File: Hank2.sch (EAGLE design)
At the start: 44 parts

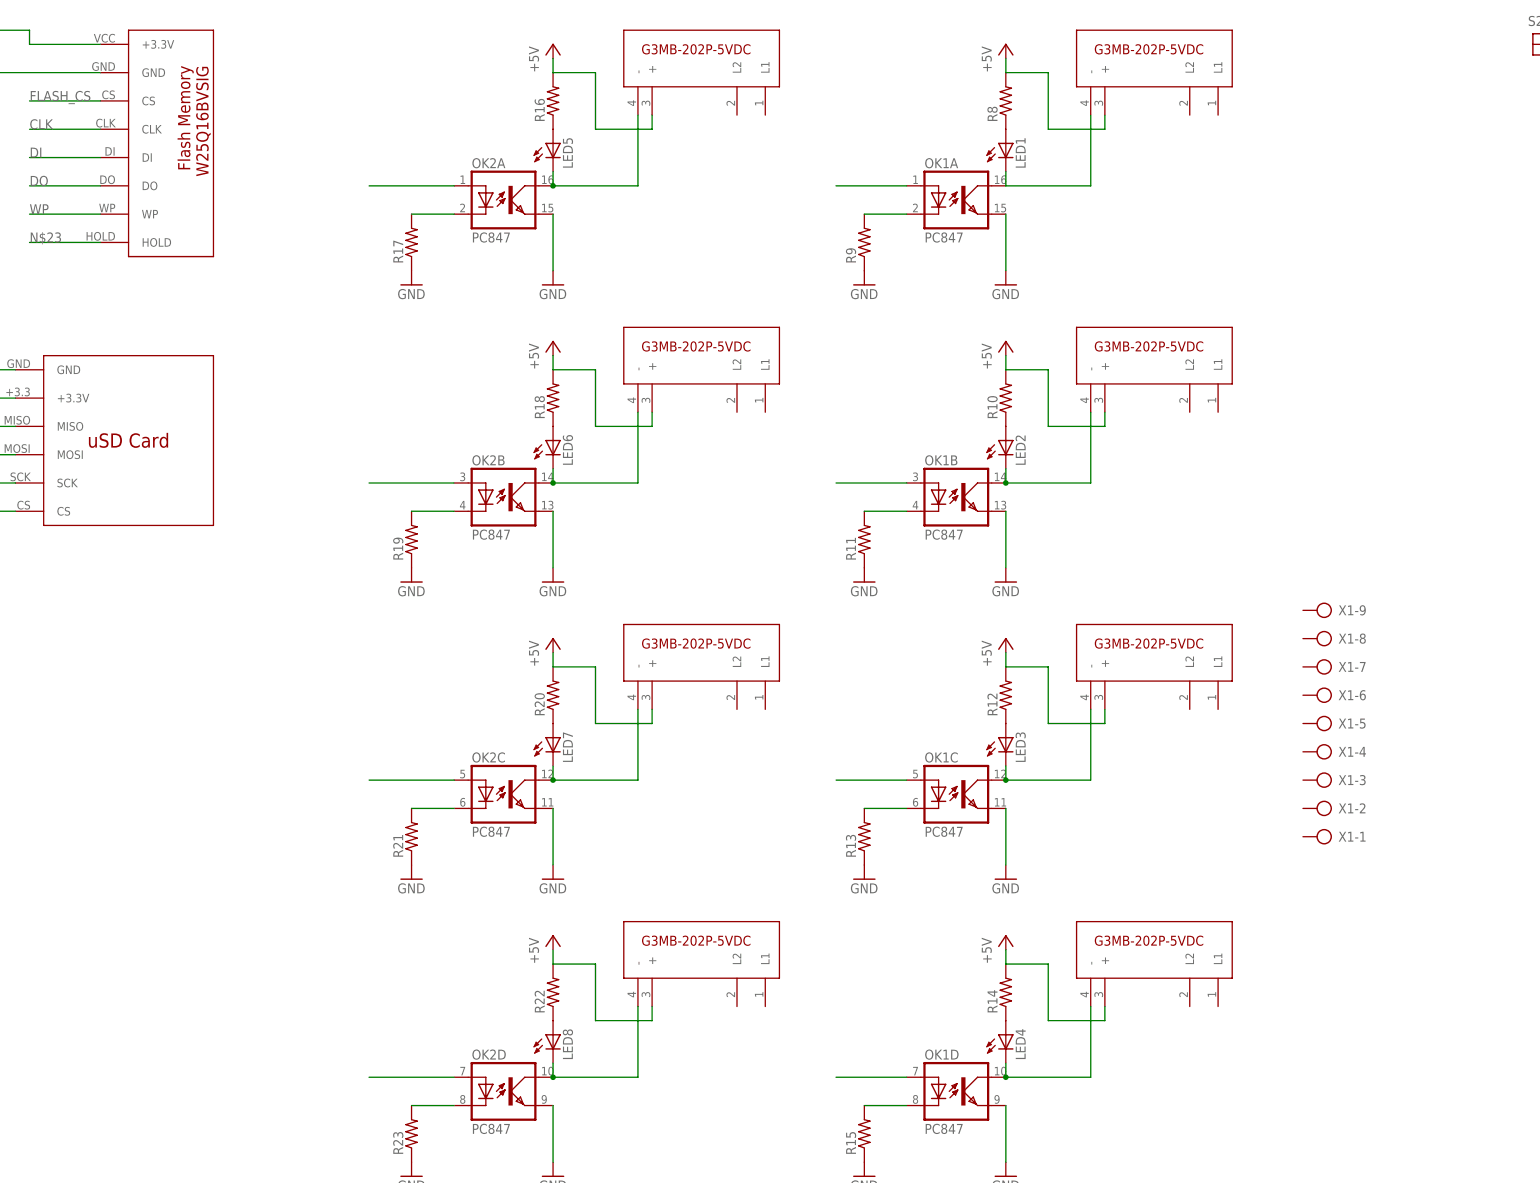
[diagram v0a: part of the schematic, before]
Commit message: Wired SSR circuits
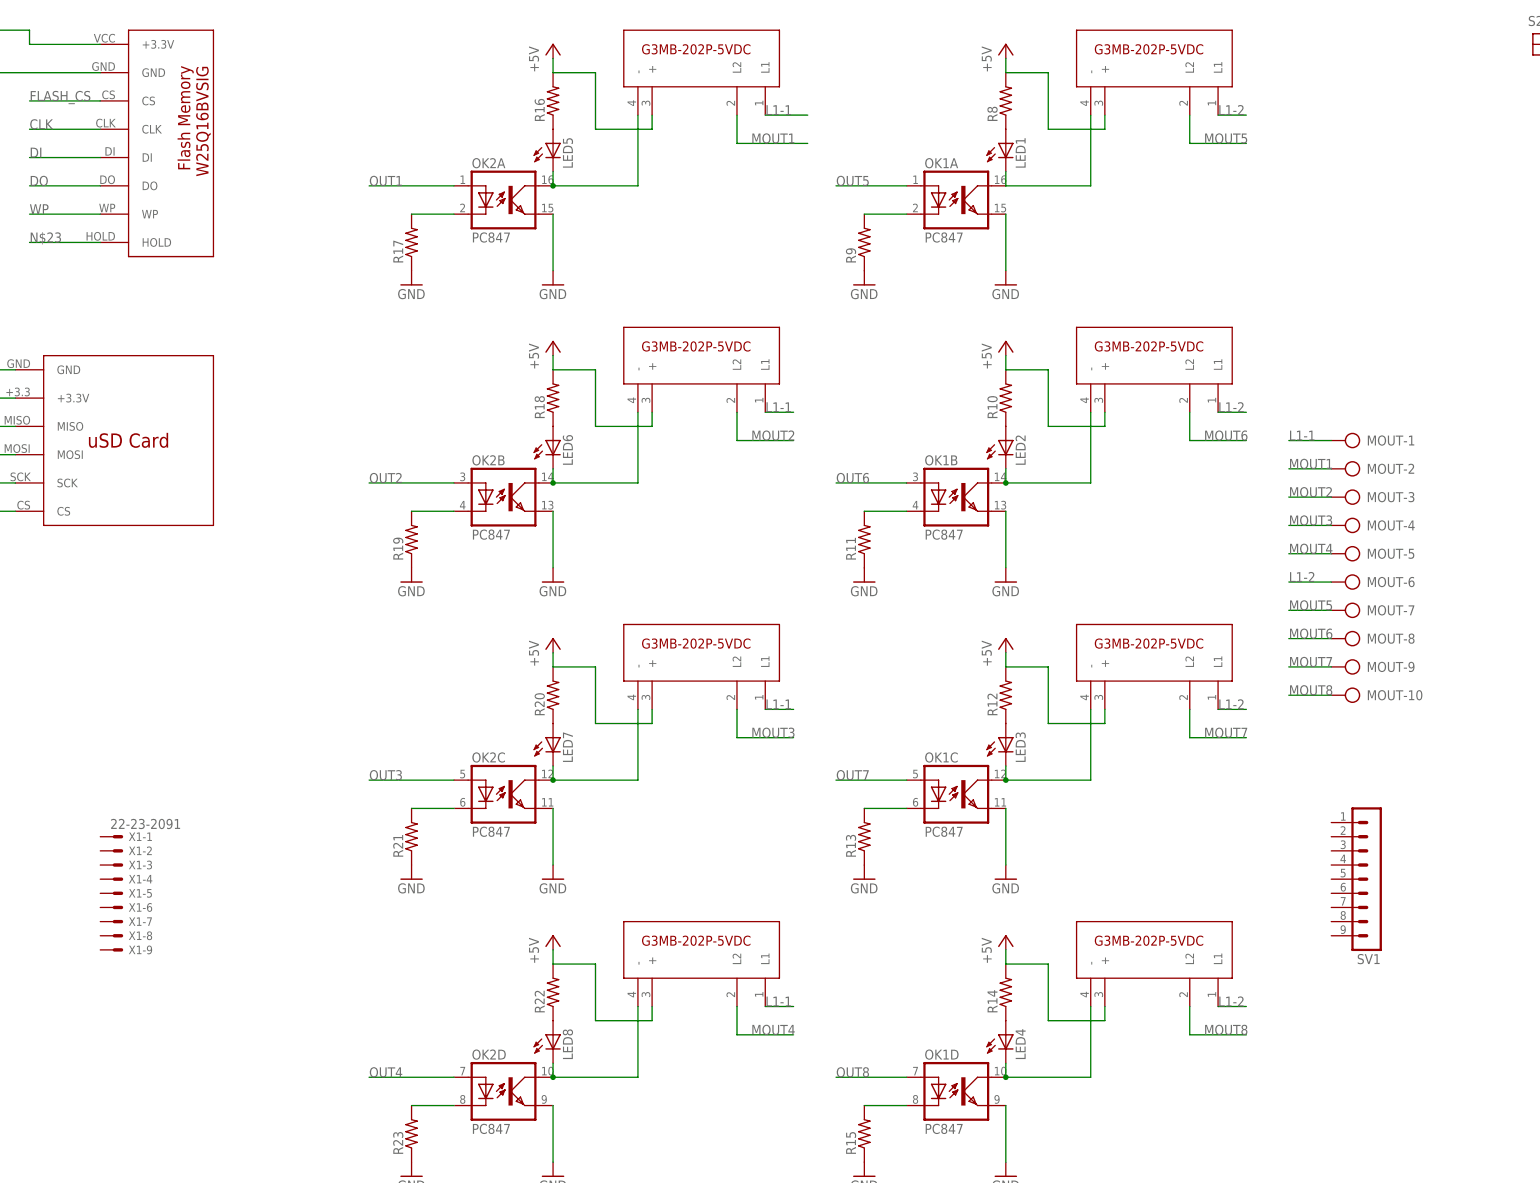
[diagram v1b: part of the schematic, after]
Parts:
- added MOUT: (no value), con-ptr500:AK300/10
- added SV1: (no value), con-lstb:MA09-1
- X1: value (none) -> 22-23-2091; device con-ptr500:AK300/9 -> con-molex:22-23-2091
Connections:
- net N$14 renamed OUT5
- net N$18 renamed OUT6
- net N$22 renamed OUT7
- net N$27 renamed OUT8
- net N$31 renamed OUT1
- net N$35 renamed OUT2
- net N$39 renamed OUT3
- net N$43 renamed OUT4
- new net L1-1: MOUT-1.KL, U$19.L1, U$20.L1, U$21.L1, U$22.L1
- new net L1-2: MOUT-6.KL, U$16.L1, U$17.L1, U$18.L1, U$8.L1
- new net MOUT1: MOUT-2.KL, U$19.L2
- new net MOUT2: MOUT-3.KL, U$20.L2
- new net MOUT3: MOUT-4.KL, U$21.L2
- new net MOUT4: MOUT-5.KL, U$22.L2
- new net MOUT5: MOUT-7.KL, U$8.L2
- new net MOUT6: MOUT-8.KL, U$16.L2
- new net MOUT7: MOUT-9.KL, U$17.L2
- new net MOUT8: MOUT-10.KL, U$18.L2
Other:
- moved on the sheet: X1-1, X1-2, X1-3, X1-4, X1-5, X1-6, X1-7, X1-8, X1-9

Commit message: Added microcontroller connections
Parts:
- added C1: 1000u, rcl:CPOL-USE5-8.5
- added C2: 0.1uF, rcl:C-US025-024X044
- added MIN, SV5: (no value), con-lstb:MA09-1
- added OLED_DISPLAY: (no value), con-lstb:MA04-1
- added PSU: (no value), con-ptr500:AK300/2
- added R1: 4.7K, rcl:R-US_0204/7
- added R2, R26: (no value), rcl:R-US_0204/7
- added R24, R25, R3, R4, R5, R6, R7: 330, rcl:R-US_0204/7
- added SV2: (no value), con-lstb:MA10-1
- added TEMP_SENSOR: (no value), con-lstb:MA03-1
- added X2: 22-23-2021, con-molex:22-23-2021
- added X3: Auto_Manual, con-molex:22-23-2021
- C5, C6, C7, C8: value (none) -> 0.1uF
- R10, R12, R14, R16, R18, R22, R8: value (none) -> 1k
- R11, R13, R15, R17, R19, R21, R23, R9: value (none) -> 150
- SV1: device con-lstb:MA09-1 -> con-lstb:MA10-1
- X1: value 22-23-2091 -> 22-23-2021; device con-molex:22-23-2091 -> con-molex:22-23-2021
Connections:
- removed net CLK: U$1.CLK
- removed net DI: U$1.DI
- removed net DO: U$1.DO
- removed net N$23: U$1.HOLD
- removed net WP: U$1.WP
- new net AUTO: R2.2, SV2.10, X3-2.S
- new net FLASH_CLK: SV2.2, U$1.CLK
- new net FLASH_DI: SV2.3, U$1.DI
- new net FLASH_DO: SV2.4, U$1.DO
- new net IN1: R3.1, SV5.2
- new net IN2: R4.1, SV5.3
- new net IN3: R5.1, SV5.4
- new net IN4: R6.1, SV5.5
- new net IN5: R7.1, SV5.6
- new net IN6: R24.1, SV5.7
- new net IN7: R25.1, SV5.8
- new net IN8: R26.1, SV5.9
- new net N$1: SV1.1, X1-2.S
- new net N$14: SV1.10
- new net N$2: SV1.2, X2-2.S
- new net N$7: R24.2, R25.2, R26.2, R3.2, R4.2, R5.2, R6.2, R7.2
- new net N$8: SV5.1
- new net TEMP_SEN: R1.1, SV2.9, TEMP_SENSOR.2
- net +3V3: now also C2.1, OLED_DISPLAY.3, R1.2, TEMP_SENSOR.3, U$1.HOLD, U$1.WP, X2-1.S, X3-1.S
- net +5V: now also C1.+, PSU-1.KL, X1-1.S
- net FLASH_CS: now also SV2.1
- net GND: now also C1.-, C2.2, MIN.1, OLED_DISPLAY.4, PSU-2.KL, R2.1, SV1.3, SV1.4, SV1.5, SV1.6, TEMP_SENSOR.1
- net MISO: now also SV2.5
- net MOSI: now also SV2.6
- net OUT1: now also MIN.2
- net OUT2: now also MIN.3
- net OUT3: now also MIN.4
- net OUT4: now also MIN.5
- net OUT5: now also MIN.6
- net OUT6: now also MIN.7
- net OUT7: now also MIN.8
- net OUT8: now also MIN.9
- net SCK: now also SV2.7
- net SCL: now also OLED_DISPLAY.1
- net SDA: now also OLED_DISPLAY.2
- net SD_CS: now also SV2.8
- net SERIAL_RXD: now also SV1.7
- net SERIAL_TXD: now also SV1.8
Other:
- note added: "TO DO: -Add connections to Microcontroller -Add 3.3V Power Supply Regulator -Add 5V low drop regulator -Add Temperature Sensor +DONE: Add the SSR Circuit"
- note removed: "TO DO: -Add connections to Microcontroller -Add 3.3V Power Supply Regulator -Add 5V low drop regulator +DONE: Add the SSR Circuit"
- moved on the sheet: C7, C8, X1-1, X1-2

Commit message: Finished first draft of the schematic, started organising the PCB
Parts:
- removed C1: 1000u, rcl:CPOL-USE5-8.5
- removed LED1, LED5, LED6, LED7, LED8: (no value), led:LED3MM
- removed R10, R12, R14, R16, R18, R22, R8: 1k, rcl:R-US_0204/7
- removed R11, R13, R15, R17, R19, R21, R23, R9: 150, rcl:R-US_0204/7
- removed R20: (no value), rcl:R-US_0204/7
- removed S2: Reset, SparkFun:TAC_SWITCHSMD
- removed U$16, U$17, U$18, U$19, U$20, U$21, U$22, U$8: SSR, HankLibraries:SSR
- added 3.3V, 5V, LO1, LO5, L_O2, L_O3, L_O4: (no value), led:LED3MM
- added CP01, CP13, CP21: 100u, rcl:CPOL-USE5-8.5
- added CP02, CP14, CP22: 100n, rcl:CPOL-USE5-8.5
- added F1, F2, F3, F4, F5, F6, F7, F8: SM 092 A0 2A, fuse:FUSEPICOFUSE
- added LF33CV, LF50ABV: (no value), v-reg:78XXL
- added PR_3.3V, PR_5V, R62, RO12, RO22, RO42, RO52, RO72, RO82: 1k, rcl:R-US_0204/7
- added R51, R61, RO11, RO21, RO31, RO41, RO71, RO81: 150, rcl:R-US_0204/7
- added RO32: (no value), rcl:R-US_0204/7
- added SSR1, SSR2, SSR3, SSR4, SSR5, SSR6, SSR7, SSR8: SSR, HankLibraries:SSR
- renumbered C2 to C_OLED, C5 to C_BT, C6 to C_FM, C7 to C_USD, C8 to C_RTC, R1 to R_TEMP, R24 to RI6, R25 to RI7, R26 to RI8, R3 to RI1, R4 to RI2, R5 to RI3, R6 to RI4, R7 to RI5
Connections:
- removed net MOUT1: MOUT-2.KL, U$19.L2
- removed net N$34: LED6.C, OK2B.COL, U$20.-
- removed net N$38: LED7.C, OK2C.COL, U$21.-
- removed net RESET: S2.3, S2.4
- new net CP12: CP01.+, CP02.+, LF33CV.IN, LF50ABV.IN, PSU-1.KL
- new net L_O1: L_O2.C, OK1B.COL, SSR2.-
- new net L_O3: L_O3.C, OK1C.COL, SSR3.-
- new net MO1: F1.2, MOUT-2.KL
- new net MO2: F2.2, MOUT-3.KL
- new net MO3: F3.2, MOUT-4.KL
- new net MO4: F4.2, MOUT-5.KL
- new net MO5: F5.2, MOUT-7.KL
- new net MO6: F6.2, MOUT-8.KL
- new net MO7: F7.2, MOUT-9.KL
- new net MO8: F8.2, MOUT-10.KL
- new net N$3: F1.1, SSR1.L2
- new net N$4: 5V.C, PR_5V.2
- new net N$5: 3.3V.C, PR_3.3V.2
- net +3V3: now also 3.3V.A, CP21.+, CP22.+, LF33CV.OUT
- net +5V: now also 5V.A, CP13.+, CP14.+, LF50ABV.OUT, R62.2, RO12.2, RO22.2, RO32.2, RO42.2, RO52.2, RO72.2, RO82.2, SSR1.+, SSR2.+, SSR3.+, SSR4.+, SSR5.+, SSR6.+, SSR7.+, SSR8.+; no longer C1.+, PSU-1.KL, R10.2, R12.2, R14.2, R16.2, R18.2, R20.2, R22.2, R8.2, U$16.+, U$17.+, U$18.+, U$19.+, U$20.+, U$21.+, U$22.+, U$8.+
- net GND: now also CP01.-, CP02.-, CP13.-, CP14.-, CP21.-, CP22.-, LF33CV.GND, LF50ABV.GND, PR_3.3V.1, PR_5V.1, R51.1, R61.1, RO11.1, RO21.1, RO31.1, RO41.1, RO71.1, RO81.1; no longer C1.-, R11.1, R13.1, R15.1, R17.1, R19.1, R21.1, R23.1, R9.1, S2.1, S2.2
- net L1-1: now also SSR1.L1, SSR2.L1, SSR3.L1, SSR4.L1; no longer U$19.L1, U$20.L1, U$21.L1, U$22.L1
- net L1-2: now also SSR5.L1, SSR6.L1, SSR7.L1, SSR8.L1; no longer U$16.L1, U$17.L1, U$18.L1, U$8.L1
- net MOUT2: now also F2.1, SSR2.L2; no longer MOUT-3.KL, U$20.L2
- net MOUT3: now also F3.1, SSR3.L2; no longer MOUT-4.KL, U$21.L2
- net MOUT4: now also F4.1, SSR4.L2; no longer MOUT-5.KL, U$22.L2
- net MOUT5: now also F5.1, SSR5.L2; no longer MOUT-7.KL, U$8.L2
- net MOUT6: now also F6.1, SSR6.L2; no longer MOUT-8.KL, U$16.L2
- net MOUT7: now also F7.1, SSR7.L2; no longer MOUT-9.KL, U$17.L2
- net MOUT8: now also F8.1, SSR8.L2; no longer MOUT-10.KL, U$18.L2
- net N$11: now also LO5.A, RO52.1; no longer LED1.A, R8.1
- net N$12: now also LO5.C, OK2A.COL, SSR5.-; no longer LED1.C, OK1A.COL, U$8.-
- net N$15: now also OK2A.C, R51.2; no longer OK1A.C, R9.2
- net N$16: now also R62.1; no longer R10.1
- net N$17: now also OK2B.COL, SSR6.-; no longer OK1B.COL, U$16.-
- net N$19: now also OK2B.C, R61.2; no longer OK1B.C, R11.2
- net N$20: now also RO72.1; no longer R12.1
- net N$21: now also OK2C.COL, SSR7.-; no longer OK1C.COL, U$17.-
- net N$24: now also OK2C.C, RO71.2; no longer OK1C.C, R13.2
- net N$25: now also RO82.1; no longer R14.1
- net N$26: now also OK2D.COL, SSR8.-; no longer OK1D.COL, U$18.-
- net N$28: now also OK2D.C, RO81.2; no longer OK1D.C, R15.2
- net N$29: now also LO1.A, RO12.1; no longer LED5.A, R16.1
- net N$30: now also LO1.C, OK1A.COL, SSR1.-; no longer LED5.C, OK2A.COL, U$19.-
- net N$32: now also OK1A.C, RO11.2; no longer OK2A.C, R17.2
- net N$33: now also L_O2.A, RO22.1; no longer LED6.A, R18.1
- net N$36: now also OK1B.C, RO21.2; no longer OK2B.C, R19.2
- net N$37: now also L_O3.A, RO32.1; no longer LED7.A, R20.1
- net N$40: now also OK1C.C, RO31.2; no longer OK2C.C, R21.2
- net N$41: now also L_O4.A, RO42.1; no longer LED8.A, R22.1
- net N$42: now also L_O4.C, OK1D.COL, SSR4.-; no longer LED8.C, OK2D.COL, U$22.-
- net N$44: now also OK1D.C, RO41.2; no longer OK2D.C, R23.2
- net OUT1: now also OK1A.A; no longer OK2A.A
- net OUT2: now also OK1B.A; no longer OK2B.A
- net OUT3: now also OK1C.A; no longer OK2C.A
- net OUT4: now also OK1D.A; no longer OK2D.A
- net OUT5: now also OK2A.A; no longer OK1A.A
- net OUT6: now also OK2B.A; no longer OK1B.A
- net OUT7: now also OK2C.A; no longer OK1C.A
- net OUT8: now also OK2D.A; no longer OK1D.A
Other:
- note added: "Fish tank controller breakout board"
- note added: "TO DO: +DONE Add connections to Microcontroller -Add 3.3V Power Supply Regulator -Add 5V low drop regulator +DONE: Add Temperature Sensor +DONE: Add the SSR Circuit -Add Fuses SM 092 A0 2A--- RS PN: 116-114"
- note added: "https://github.com/FreeRangeLobster/FishHank"
- note removed: "Arduino Pro Mini Design by Spark Fun Electronics"
- note removed: "TO DO: -Add connections to Microcontroller -Add 3.3V Power Supply Regulator -Add 5V low drop regulator -Add Temperature Sensor +DONE: Add the SSR Circuit"
- note removed: "http://creativecommons.org/licenses/by-sa/3.0"
- moved on the sheet: LED2, LED3, LED4, MOUT-1, MOUT-10, MOUT-2, MOUT-3, MOUT-4, MOUT-5, MOUT-6, MOUT-7, MOUT-8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

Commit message: Placed components in PCB and exported some pics to verify footprints
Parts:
- renumbered CP13 to CP51, CP14 to CP52, CP21 to CP31, CP22 to CP32, LED2 to LO6, LED3 to LO7, LED4 to LO8, SV5 to IN_BUTTONS, X1 to JUM_3.3V, X2 to JUM_5.5V
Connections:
- removed net N$8: IN_BUTTONS.1
- net +3V3: now also IN_BUTTONS.1
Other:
- note added: "TO DO: +DONE Add connections to Microcontroller -Add 3.3V Power Supply Regulator -Add 5V low drop regulator +DONE: Add Temperature Sensor +DONE: Add the SSR Circuit -DONE:Add Fuses SM 092 A0 2A--- RS PN: 116-114 -Add Connector with 8Inputs"
- note removed: "TO DO: +DONE Add connections to Microcontroller -Add 3.3V Power Supply Regulator -Add 5V low drop regulator +DONE: Add Temperature Sensor +DONE: Add the SSR Circuit -Add Fuses SM 092 A0 2A--- RS PN: 116-114"

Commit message: Changed the interface of the SSR to Arduino. Added Arduino Sketch
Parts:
- removed MIN: (no value), con-lstb:MA09-1
- removed OK1, OK2: PC847, optocoupler:PC847
- added ARDUINO: ARDUINO_MICRO, HankLibraries:ARDUINO_MICRO
- added RO13, RO23, RO43, RO53, RO73, RO83: 1k, rcl:R-US_0204/7
- added RO33: (no value), rcl:R-US_0204/7
- added RO62: 10K, rcl:R-US_0204/7
- added T1, T2, T3, T4, T5, T6, T7, T8: 2n2222, transistor:2SC458
- R51, R61, RO11, RO71: value 150 -> 10K
- RO12, RO22, RO42, RO52, RO72, RO82: value 1k -> 10K
- RO32: value (none) -> 10K
- RO41, RO81: value 150 -> 10k
- renumbered R62 to RO63
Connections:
- removed net AUTO: R2.2, SV2.10, X3-2.S
- removed net N$32: OK1A.C, RO11.2
- new net AUTO_MANUAL: ARDUINO.10, R2.2, SV2.10, X3-2.S
- new net N$18: RO62.1, T7.B
- new net N$22: RO72.1, T6.B
- new net N$23: RO42.1, T4.B
- new net N$27: RO32.1, T3.B
- new net N$31: RO22.1, T2.B
- new net N$34: RO82.1, T5.B
- new net N$35: ARDUINO.20
- new net N$6: ARDUINO.21
- new net N$8: RO12.1, T1.B
- new net N$9: RO52.1, T8.B
- net +5V: now also ARDUINO.VIN, RO13.2, RO23.2, RO33.2, RO43.2, RO53.2, RO73.2, RO83.2; no longer RO12.2, RO22.2, RO32.2, RO42.2, RO52.2, RO72.2, RO82.2
- net GND: now also ARDUINO.GND1, ARDUINO.GND2, T3.E; no longer MIN.1, OK1A.EMIT, OK1B.EMIT, OK1C.EMIT, OK1D.EMIT, OK2A.EMIT, OK2B.EMIT, OK2C.EMIT, OK2D.EMIT
- net IN1: now also ARDUINO.36
- net IN2: now also ARDUINO.37
- net IN3: now also ARDUINO.38
- net IN4: now also ARDUINO.39
- net IN5: now also ARDUINO.40
- net IN6: now also ARDUINO.41
- net IN7: now also ARDUINO.11
- net IN8: now also ARDUINO.9
- net L_O1: now also T2.C; no longer OK1B.COL
- net L_O3: now also T3.C; no longer OK1C.COL
- net N$11: now also RO53.1; no longer RO52.1
- net N$12: now also T8.C; no longer OK2A.COL
- net N$15: now also RO52.2; no longer OK2A.C
- net N$17: now also T7.C; no longer OK2B.COL
- net N$19: now also RO62.2; no longer OK2B.C
- net N$20: now also RO73.1; no longer RO72.1
- net N$21: now also T6.C; no longer OK2C.COL
- net N$24: now also RO72.2; no longer OK2C.C
- net N$25: now also RO83.1; no longer RO82.1
- net N$26: now also T5.C; no longer OK2D.COL
- net N$28: now also RO82.2; no longer OK2D.C
- net N$29: now also RO13.1; no longer RO12.1
- net N$30: now also T1.C; no longer OK1A.COL
- net N$33: now also RO23.1; no longer RO22.1
- net N$36: now also RO22.2; no longer OK1B.C
- net N$37: now also RO33.1; no longer RO32.1
- net N$40: now also RO32.2; no longer OK1C.C
- net N$41: now also RO43.1; no longer RO42.1
- net N$42: now also T4.C; no longer OK1D.COL
- net N$44: now also RO42.2; no longer OK1D.C
- net OUT1: now also ARDUINO.32, RO11.2, RO12.2; no longer MIN.2, OK1A.A
- net OUT2: now also ARDUINO.26; no longer MIN.3, OK1B.A
- net OUT3: now also ARDUINO.12; no longer MIN.4, OK1C.A
- net OUT4: now also ARDUINO.30; no longer MIN.5, OK1D.A
- net OUT5: now also ARDUINO.29; no longer MIN.6, OK2A.A
- net OUT6: now also ARDUINO.27; no longer MIN.7, OK2B.A
- net OUT7: now also ARDUINO.31; no longer MIN.8, OK2C.A
- net OUT8: now also ARDUINO.18; no longer MIN.9, OK2D.A
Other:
- moved on the sheet: IN_BUTTONS, R51, R61, RI1, RI2, RI3, RI4, RI5, RI6, RI7, RI8, RO11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
